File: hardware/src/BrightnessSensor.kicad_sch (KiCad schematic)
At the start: 0 parts

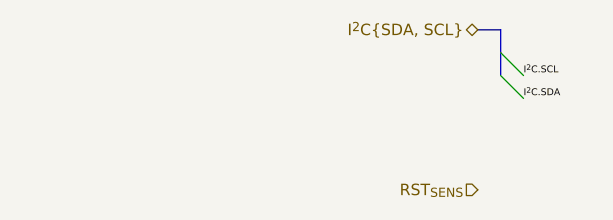
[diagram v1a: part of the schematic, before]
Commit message: Mod: RTC GPIOs
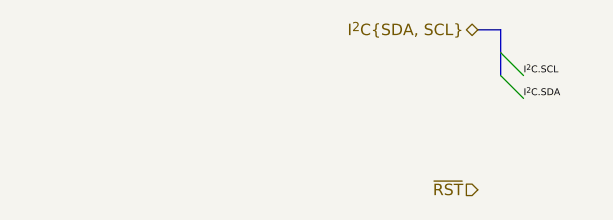
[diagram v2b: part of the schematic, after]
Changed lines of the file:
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@@
 	(title_block
 		(title "Wordclock - Brightness Sensor")
-		(date "2024-10-19")
+		(date "2024-10-20")
 		(rev "A")
 		(company "ElektroNik Zoller")
@@
 		)
 	)
-	(hierarchical_label "RST_{SENS}"
+	(hierarchical_label "~{RST}"
 		(shape input)
 		(at 165.1 81.28 180)

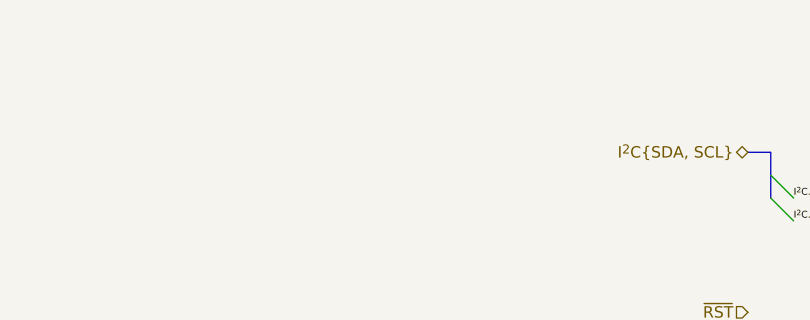
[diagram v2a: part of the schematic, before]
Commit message: Add: Text Headers to the indidual schematic regions
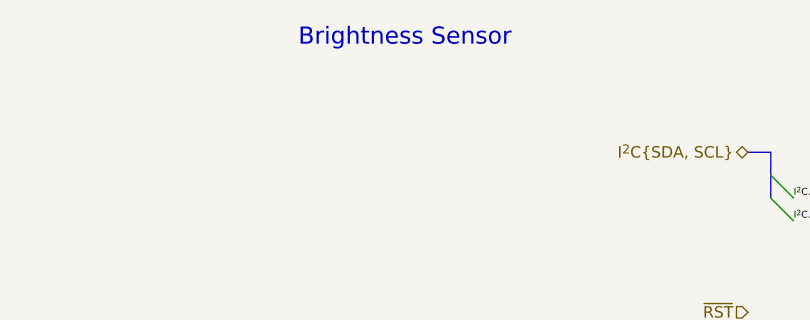
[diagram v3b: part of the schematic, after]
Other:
- note added: "Brightness Sensor"
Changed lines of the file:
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@@
+		)
+	)
+	(text "Brightness Sensor"
+		(exclude_from_sim no)
+		(at 127 50.8 0)
+		(effects
+			(font
+				(size 1.905 1.905)
+			)
 		)
 	)

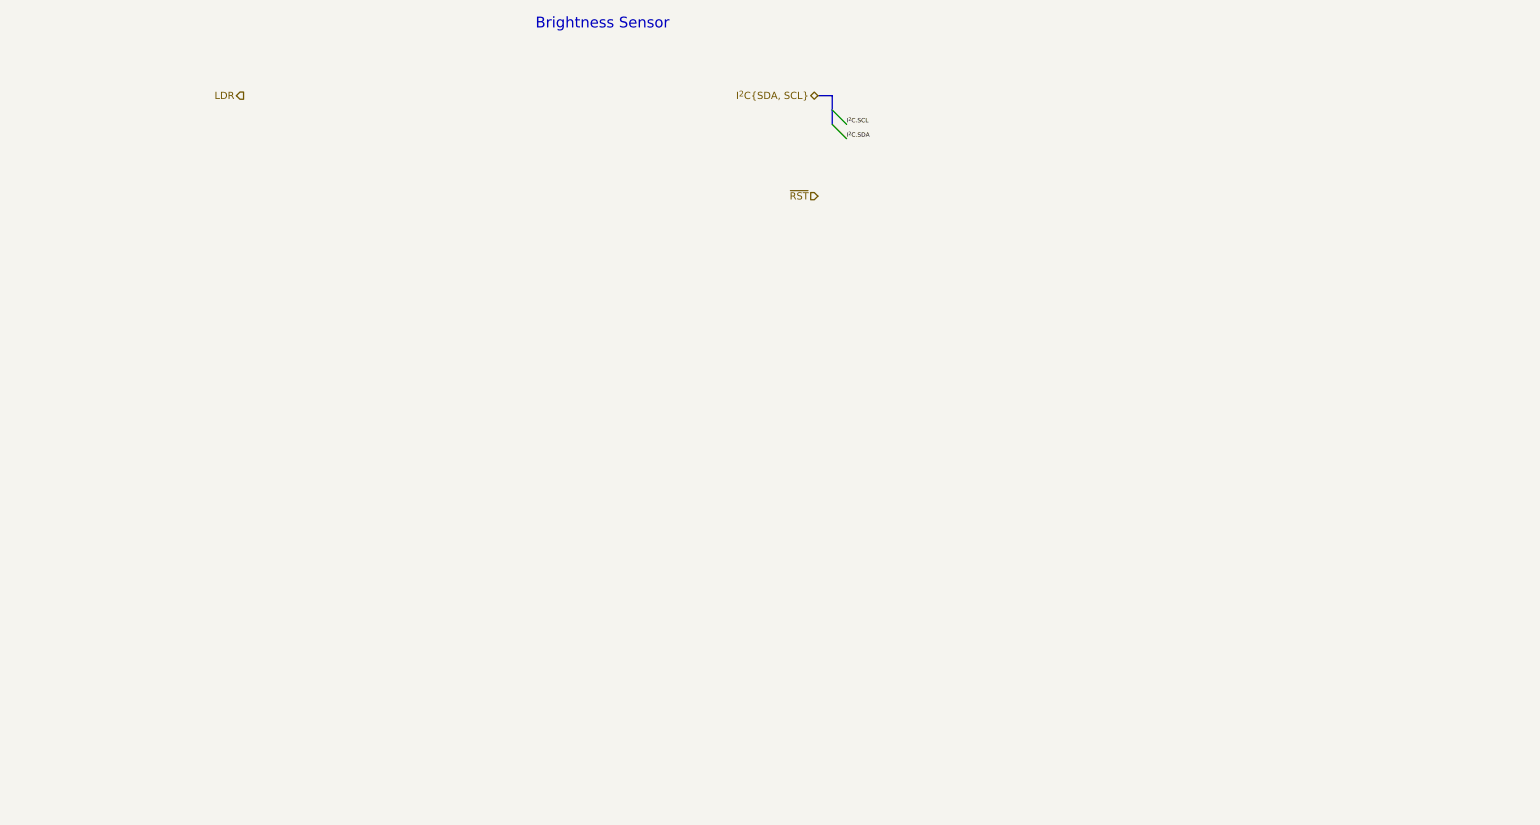
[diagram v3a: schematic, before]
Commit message: Add: Brightness sensors to the schematic
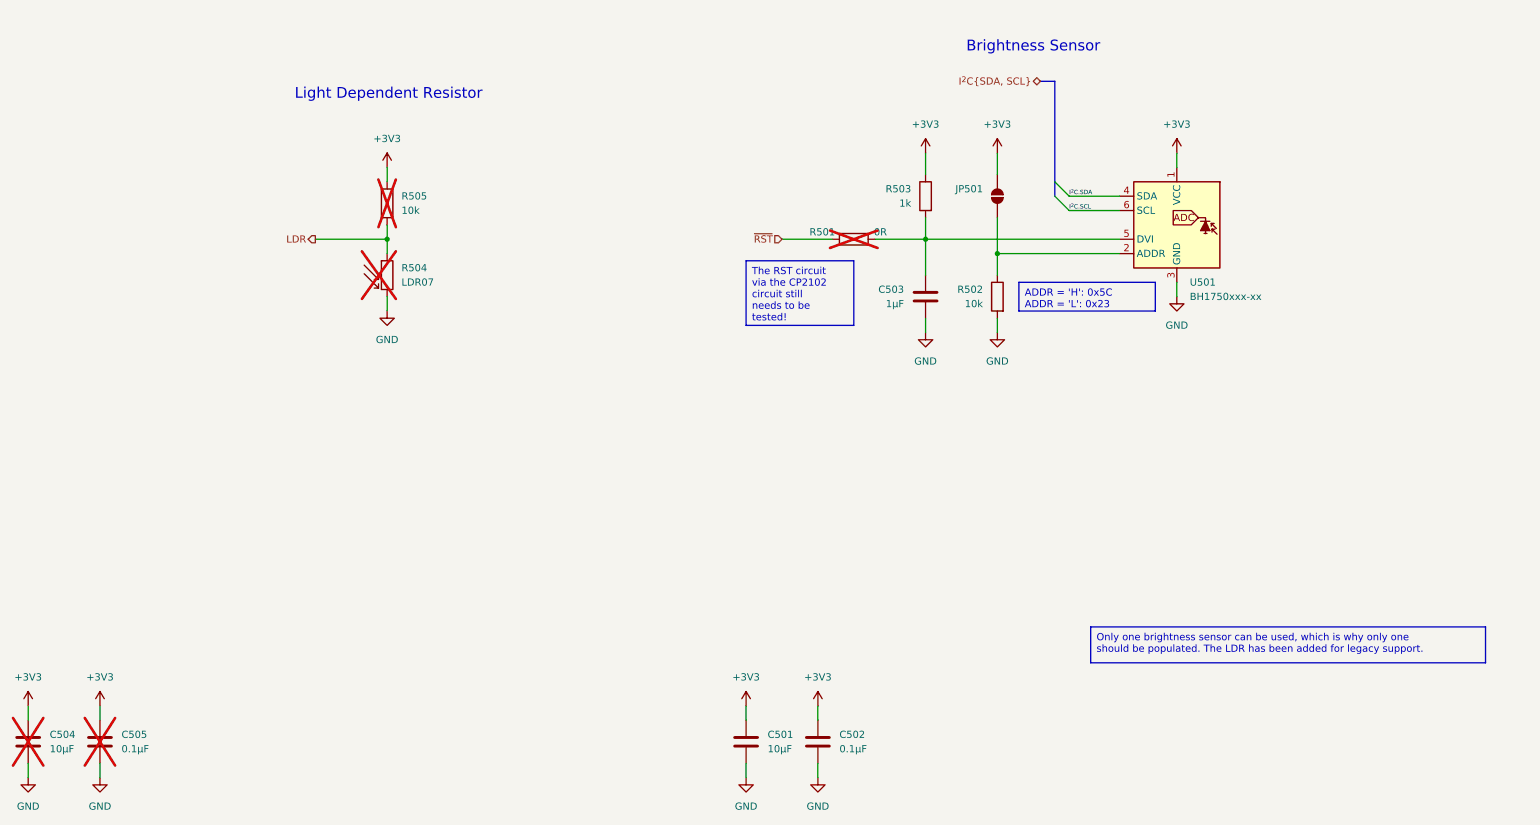
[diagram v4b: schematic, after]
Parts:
- added C501, C504: 10µF, symbol Device:C
- added C502, C505: 0.1µF, symbol Device:C
- added C503: 1µF, symbol Device:C
- added JP501: SolderJumper_2_Open, Jumper:SolderJumper-2_P1.3mm_Open_RoundedPad1.0x1.5mm, symbol Jumper:SolderJumper_2_Open
- added R501: 0R, symbol Device:R
- added R502, R505: 10k, symbol Device:R
- added R503: 1k, symbol Device:R
- added R504: LDR07, OptoDevice:R_LDR_5.1x4.3mm_P3.4mm_Vertical, symbol Sensor_Optical:LDR07
- added U501: BH1750xxx-xx, Package_TO_SOT_SMD:HVSOF6, symbol Sensor_Optical_User:BH1750xxx-xx
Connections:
- net I^{2}C.SCL: now also U501.6 (SCL)
- net I^{2}C.SDA: now also U501.4 (SDA)
- net LDR: now also R504.1, R505.2
- net ~{RST}: now also R501.2
- new net: C503.1, R501.1, R503.2, U501.5 (DVI)
- new net: JP501.1 (A), R502.1, U501.2 (ADDR)
- new net +3V3: C501.1, C502.1, C504.1, C505.1, JP501.2 (B), R503.1, R505.1, U501.1 (VCC)
- new net GND: C501.2, C502.2, C503.2, C504.2, C505.2, R502.2, R504.2, U501.3 (GND)
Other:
- note added: "Light Dependent Resistor"
